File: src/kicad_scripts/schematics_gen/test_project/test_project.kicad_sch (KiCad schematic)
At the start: 102 parts

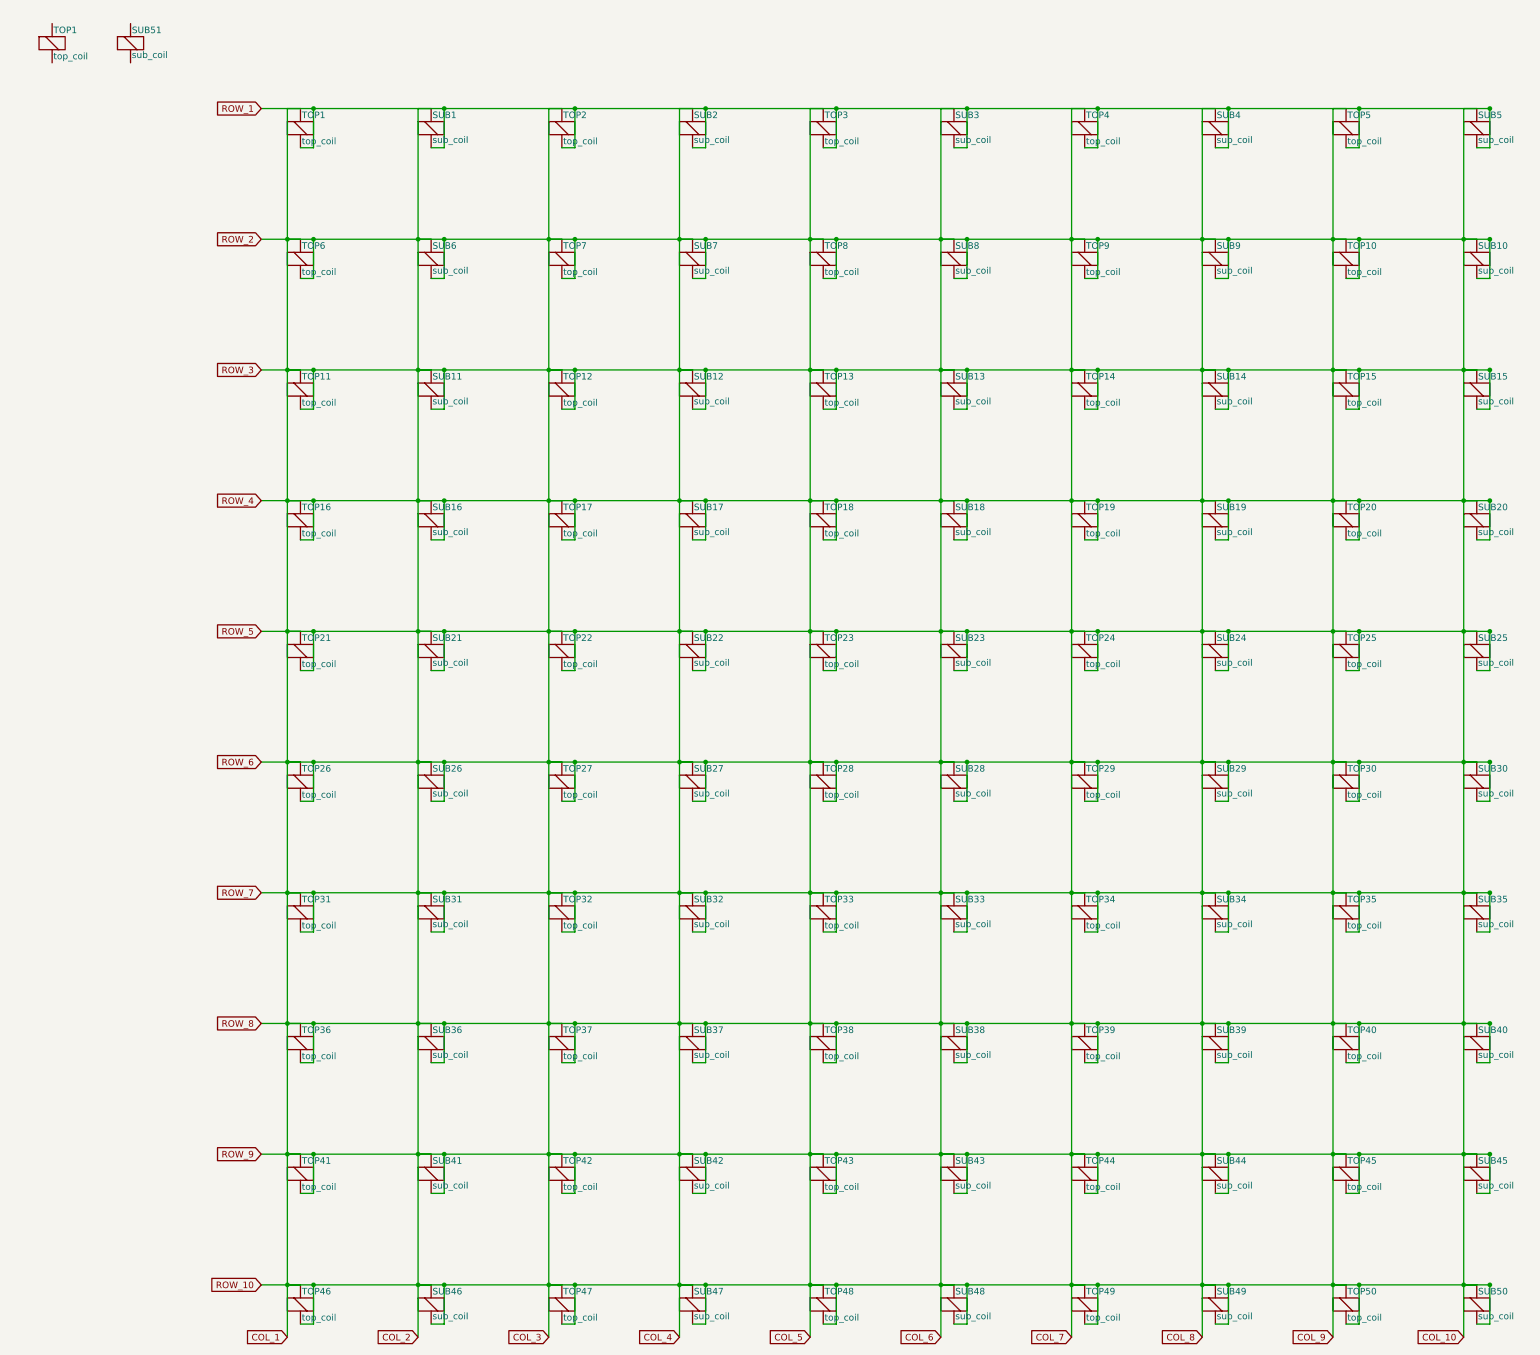
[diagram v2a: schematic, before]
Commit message: Working component matrix schematics drawer
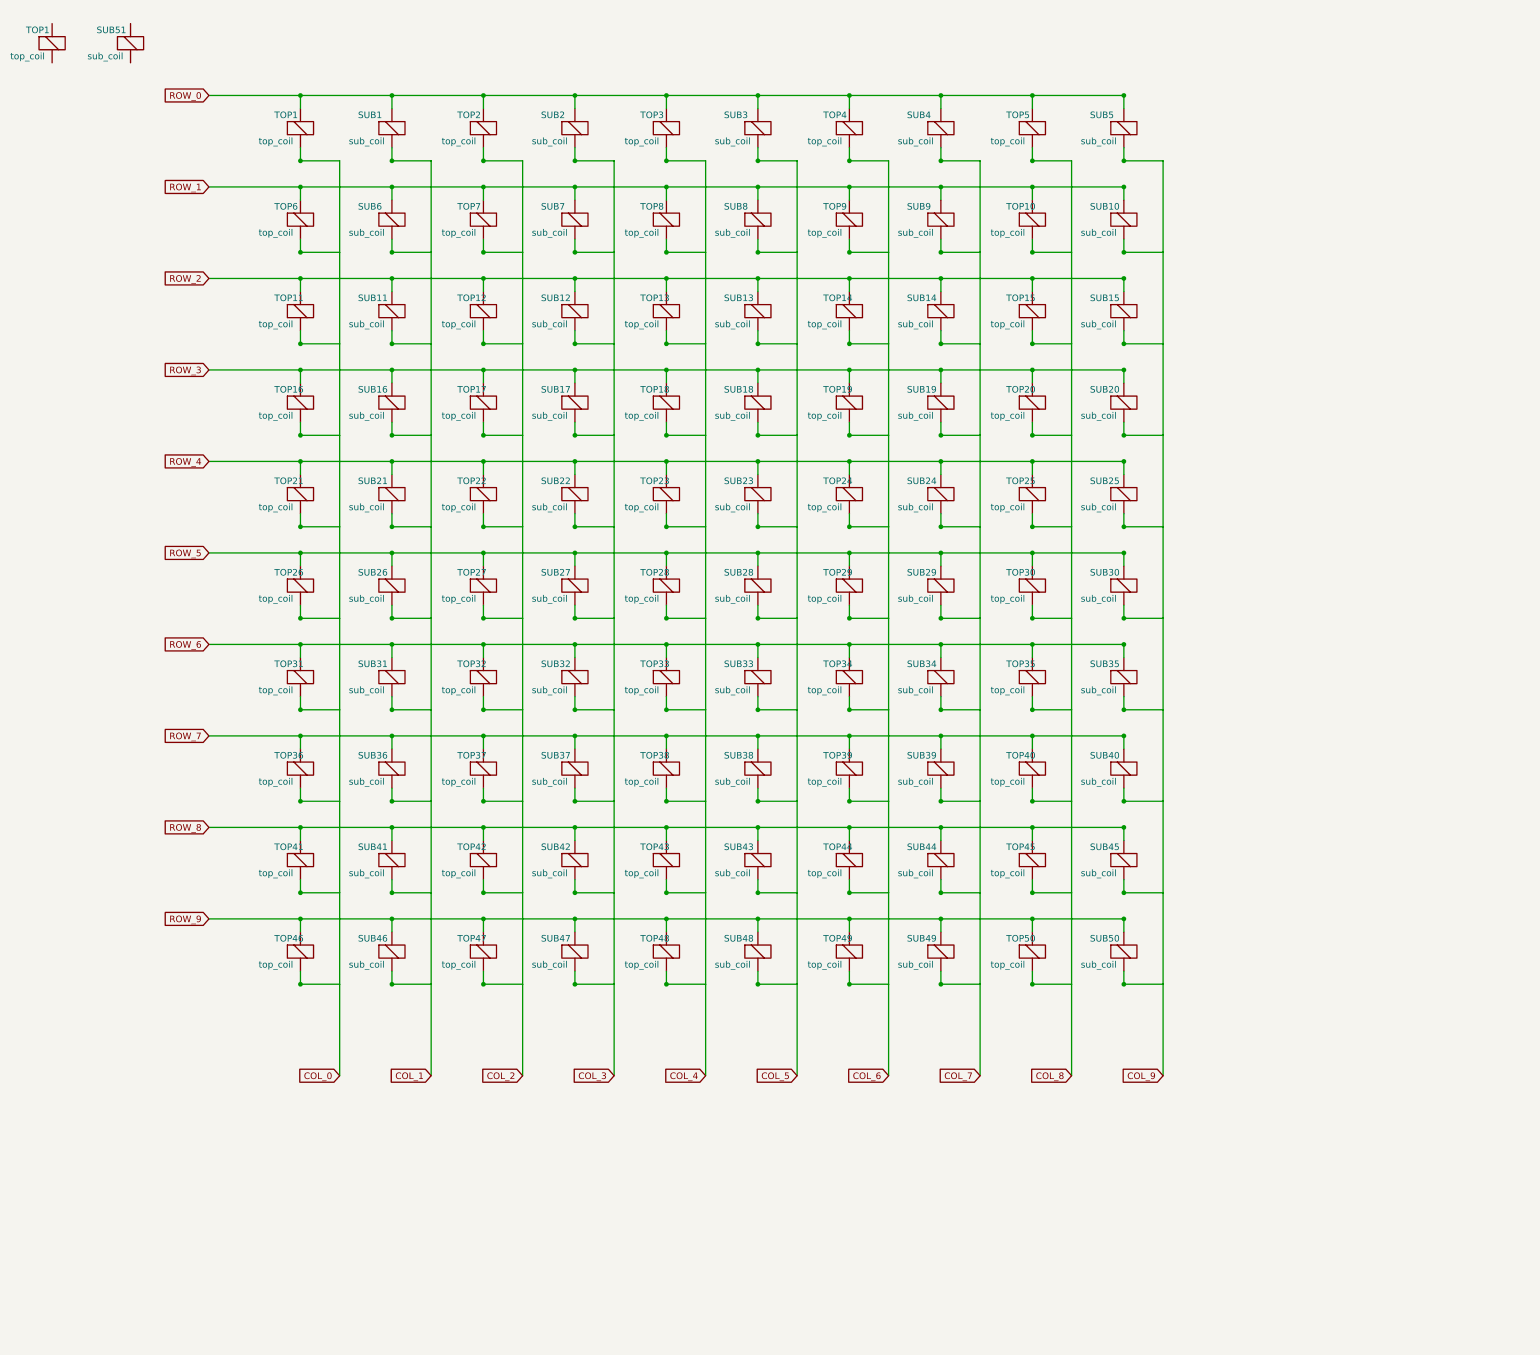
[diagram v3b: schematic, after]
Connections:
- net COL_1: no longer SUB1.1 (A), SUB10.1 (A), SUB10.2 (B), SUB11.1 (A), SUB12.1 (A), SUB12.2 (B), SUB13.1 (A), SUB13.2 (B), SUB14.1 (A), SUB14.2 (B), SUB15.1 (A), SUB15.2 (B), SUB16.1 (A), SUB17.1 (A), SUB17.2 (B), SUB18.1 (A), SUB18.2 (B), SUB19.1 (A), SUB19.2 (B), SUB2.1 (A), SUB2.2 (B), SUB20.1 (A), SUB20.2 (B), SUB21.1 (A), SUB22.1 (A), SUB22.2 (B), SUB23.1 (A), SUB23.2 (B), SUB24.1 (A), SUB24.2 (B), SUB25.1 (A), SUB25.2 (B), SUB26.1 (A), SUB27.1 (A), SUB27.2 (B), SUB28.1 (A), SUB28.2 (B), SUB29.1 (A), SUB29.2 (B), SUB3.1 (A), SUB3.2 (B), SUB30.1 (A), SUB30.2 (B), SUB31.1 (A), SUB32.1 (A), SUB32.2 (B), SUB33.1 (A), SUB33.2 (B), SUB34.1 (A), SUB34.2 (B), SUB35.1 (A), SUB35.2 (B), SUB36.1 (A), SUB37.1 (A), SUB37.2 (B), SUB38.1 (A), SUB38.2 (B), SUB39.1 (A), SUB39.2 (B), SUB4.1 (A), SUB4.2 (B), SUB40.1 (A), SUB40.2 (B), SUB41.1 (A), SUB42.1 (A), SUB42.2 (B), SUB43.1 (A), SUB43.2 (B), SUB44.1 (A), SUB44.2 (B), SUB45.1 (A), SUB45.2 (B), SUB46.1 (A), SUB47.1 (A), SUB47.2 (B), SUB48.1 (A), SUB48.2 (B), SUB49.1 (A), SUB49.2 (B), SUB5.1 (A), SUB5.2 (B), SUB50.1 (A), SUB50.2 (B), SUB6.1 (A), SUB7.1 (A), SUB7.2 (B), SUB8.1 (A), SUB8.2 (B), SUB9.1 (A), SUB9.2 (B), TOP1.1 (A), TOP1.2 (B), TOP10.1 (A), TOP10.2 (B), TOP11.1 (A), TOP11.2 (B), TOP12.1 (A), TOP12.2 (B), TOP13.1 (A), TOP13.2 (B), TOP14.1 (A), TOP14.2 (B), TOP15.1 (A), TOP15.2 (B), TOP16.1 (A), TOP16.2 (B), TOP17.1 (A), TOP17.2 (B), TOP18.1 (A), TOP18.2 (B), TOP19.1 (A), TOP19.2 (B), TOP2.1 (A), TOP2.2 (B), TOP20.1 (A), TOP20.2 (B), TOP21.1 (A), TOP21.2 (B), TOP22.1 (A), TOP22.2 (B), TOP23.1 (A), TOP23.2 (B), TOP24.1 (A), TOP24.2 (B), TOP25.1 (A), TOP25.2 (B), TOP26.1 (A), TOP26.2 (B), TOP27.1 (A), TOP27.2 (B), TOP28.1 (A), TOP28.2 (B), TOP29.1 (A), TOP29.2 (B), TOP3.1 (A), TOP3.2 (B), TOP30.1 (A), TOP30.2 (B), TOP31.1 (A), TOP31.2 (B), TOP32.1 (A), TOP32.2 (B), TOP33.1 (A), TOP33.2 (B), TOP34.1 (A), TOP34.2 (B), TOP35.1 (A), TOP35.2 (B), TOP36.1 (A), TOP36.2 (B), TOP37.1 (A), TOP37.2 (B), TOP38.1 (A), TOP38.2 (B), TOP39.1 (A), TOP39.2 (B), TOP4.1 (A), TOP4.2 (B), TOP40.1 (A), TOP40.2 (B), TOP41.1 (A), TOP41.2 (B), TOP42.1 (A), TOP42.2 (B), TOP43.1 (A), TOP43.2 (B), TOP44.1 (A), TOP44.2 (B), TOP45.1 (A), TOP45.2 (B), TOP46.1 (A), TOP46.2 (B), TOP47.1 (A), TOP47.2 (B), TOP48.1 (A), TOP48.2 (B), TOP49.1 (A), TOP49.2 (B), TOP5.1 (A), TOP5.2 (B), TOP50.1 (A), TOP50.2 (B), TOP6.1 (A), TOP6.2 (B), TOP7.1 (A), TOP7.2 (B), TOP8.1 (A), TOP8.2 (B), TOP9.1 (A), TOP9.2 (B)
- new net COL_0: TOP1.2 (B), TOP11.2 (B), TOP16.2 (B), TOP21.2 (B), TOP26.2 (B), TOP31.2 (B), TOP36.2 (B), TOP41.2 (B), TOP46.2 (B), TOP6.2 (B)
- new net COL_2: TOP12.2 (B), TOP17.2 (B), TOP2.2 (B), TOP22.2 (B), TOP27.2 (B), TOP32.2 (B), TOP37.2 (B), TOP42.2 (B), TOP47.2 (B), TOP7.2 (B)
- new net COL_3: SUB12.2 (B), SUB17.2 (B), SUB2.2 (B), SUB22.2 (B), SUB27.2 (B), SUB32.2 (B), SUB37.2 (B), SUB42.2 (B), SUB47.2 (B), SUB7.2 (B)
- new net COL_4: TOP13.2 (B), TOP18.2 (B), TOP23.2 (B), TOP28.2 (B), TOP3.2 (B), TOP33.2 (B), TOP38.2 (B), TOP43.2 (B), TOP48.2 (B), TOP8.2 (B)
- new net COL_5: SUB13.2 (B), SUB18.2 (B), SUB23.2 (B), SUB28.2 (B), SUB3.2 (B), SUB33.2 (B), SUB38.2 (B), SUB43.2 (B), SUB48.2 (B), SUB8.2 (B)
- new net COL_6: TOP14.2 (B), TOP19.2 (B), TOP24.2 (B), TOP29.2 (B), TOP34.2 (B), TOP39.2 (B), TOP4.2 (B), TOP44.2 (B), TOP49.2 (B), TOP9.2 (B)
- new net COL_7: SUB14.2 (B), SUB19.2 (B), SUB24.2 (B), SUB29.2 (B), SUB34.2 (B), SUB39.2 (B), SUB4.2 (B), SUB44.2 (B), SUB49.2 (B), SUB9.2 (B)
- new net COL_8: TOP10.2 (B), TOP15.2 (B), TOP20.2 (B), TOP25.2 (B), TOP30.2 (B), TOP35.2 (B), TOP40.2 (B), TOP45.2 (B), TOP5.2 (B), TOP50.2 (B)
- new net COL_9: SUB10.2 (B), SUB15.2 (B), SUB20.2 (B), SUB25.2 (B), SUB30.2 (B), SUB35.2 (B), SUB40.2 (B), SUB45.2 (B), SUB5.2 (B), SUB50.2 (B)
- new net ROW_0: SUB1.1 (A), SUB2.1 (A), SUB3.1 (A), SUB4.1 (A), SUB5.1 (A), TOP1.1 (A), TOP2.1 (A), TOP3.1 (A), TOP4.1 (A), TOP5.1 (A)
- new net ROW_1: SUB10.1 (A), SUB6.1 (A), SUB7.1 (A), SUB8.1 (A), SUB9.1 (A), TOP10.1 (A), TOP6.1 (A), TOP7.1 (A), TOP8.1 (A), TOP9.1 (A)
- new net ROW_2: SUB11.1 (A), SUB12.1 (A), SUB13.1 (A), SUB14.1 (A), SUB15.1 (A), TOP11.1 (A), TOP12.1 (A), TOP13.1 (A), TOP14.1 (A), TOP15.1 (A)
- new net ROW_3: SUB16.1 (A), SUB17.1 (A), SUB18.1 (A), SUB19.1 (A), SUB20.1 (A), TOP16.1 (A), TOP17.1 (A), TOP18.1 (A), TOP19.1 (A), TOP20.1 (A)
- new net ROW_4: SUB21.1 (A), SUB22.1 (A), SUB23.1 (A), SUB24.1 (A), SUB25.1 (A), TOP21.1 (A), TOP22.1 (A), TOP23.1 (A), TOP24.1 (A), TOP25.1 (A)
- new net ROW_5: SUB26.1 (A), SUB27.1 (A), SUB28.1 (A), SUB29.1 (A), SUB30.1 (A), TOP26.1 (A), TOP27.1 (A), TOP28.1 (A), TOP29.1 (A), TOP30.1 (A)
- new net ROW_6: SUB31.1 (A), SUB32.1 (A), SUB33.1 (A), SUB34.1 (A), SUB35.1 (A), TOP31.1 (A), TOP32.1 (A), TOP33.1 (A), TOP34.1 (A), TOP35.1 (A)
- new net ROW_7: SUB36.1 (A), SUB37.1 (A), SUB38.1 (A), SUB39.1 (A), SUB40.1 (A), TOP36.1 (A), TOP37.1 (A), TOP38.1 (A), TOP39.1 (A), TOP40.1 (A)
- new net ROW_8: SUB41.1 (A), SUB42.1 (A), SUB43.1 (A), SUB44.1 (A), SUB45.1 (A), TOP41.1 (A), TOP42.1 (A), TOP43.1 (A), TOP44.1 (A), TOP45.1 (A)
- new net ROW_9: SUB46.1 (A), SUB47.1 (A), SUB48.1 (A), SUB49.1 (A), SUB50.1 (A), TOP46.1 (A), TOP47.1 (A), TOP48.1 (A), TOP49.1 (A), TOP50.1 (A)

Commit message: Fixed scalability issue
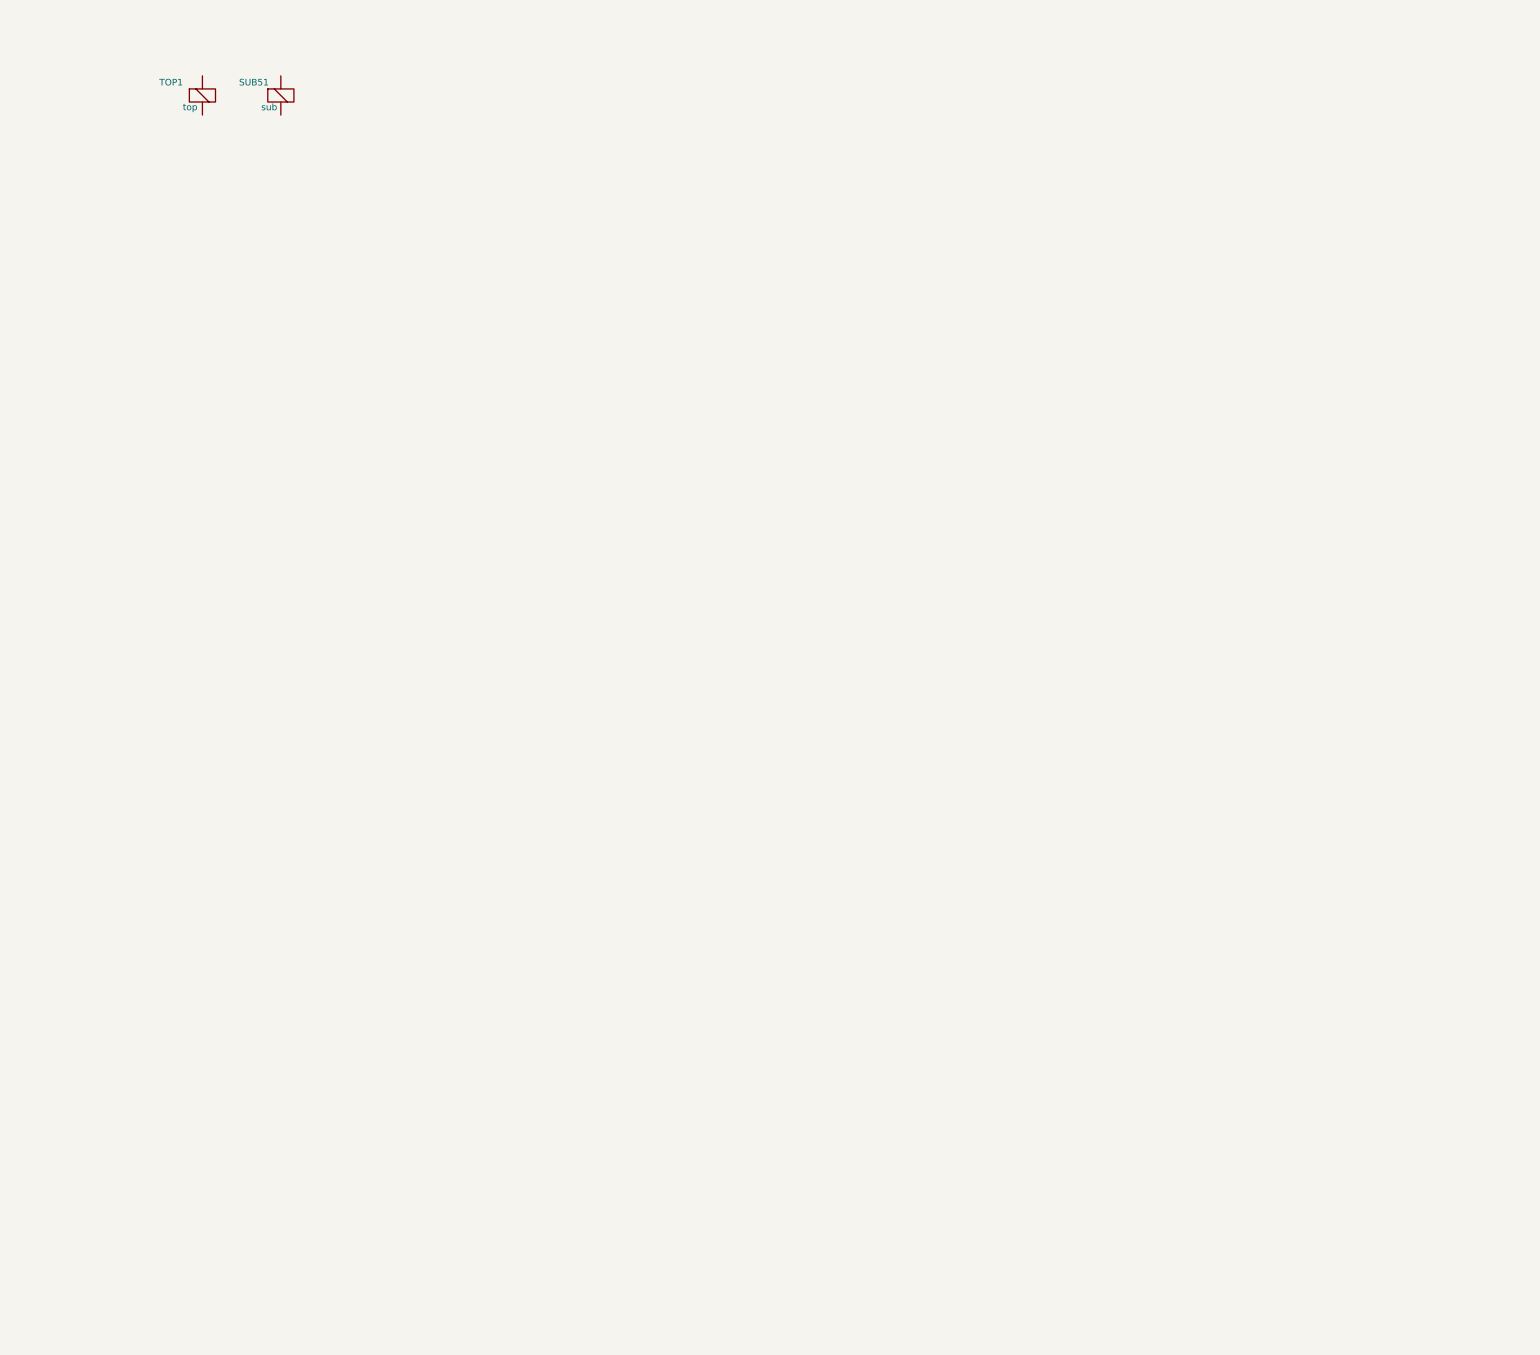
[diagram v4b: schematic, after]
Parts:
- removed SUB1, SUB10, SUB11, SUB12, SUB13, SUB14, SUB15, SUB16, SUB17, SUB18, SUB19, SUB2, SUB20, SUB21, SUB22, SUB23, SUB24, SUB25, SUB26, SUB27, SUB28, SUB29, SUB3, SUB30, SUB31, SUB32, SUB33, SUB34, SUB35, SUB36, SUB37, SUB38, SUB39, SUB4, SUB40, SUB41, SUB42, SUB43, SUB44, SUB45, SUB46, SUB47, SUB48, SUB49, SUB5, SUB50, SUB6, SUB7, SUB8, SUB9: sub_coil, sub_coils:top_coil, symbol square_coils:sub_coil
- removed TOP1, TOP10, TOP11, TOP12, TOP13, TOP14, TOP15, TOP16, TOP17, TOP18, TOP19, TOP2, TOP20, TOP21, TOP22, TOP23, TOP24, TOP25, TOP26, TOP27, TOP28, TOP29, TOP3, TOP30, TOP31, TOP32, TOP33, TOP34, TOP35, TOP36, TOP37, TOP38, TOP39, TOP4, TOP40, TOP41, TOP42, TOP43, TOP44, TOP45, TOP46, TOP47, TOP48, TOP49, TOP5, TOP50, TOP6, TOP7, TOP8, TOP9: top_coil, sub_coils:top_coil, symbol square_coils:top_coil
- SUB51: value sub_coil -> sub
- TOP1: value top_coil -> top
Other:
- moved on the sheet: SUB51, TOP1
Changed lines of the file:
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@@
+(kicad_sch
+	(version 20231120)
+	(generator "eeschema")
+	(generator_version "8.0")
+	(paper "A2")
+	(title_block
+		(date "2024-07-23")
+	)
+	(symbol
+		(lib_id "square_coils:sub_coil")
+		(at -5.08 -6.35 0)
+		(unit 1)
+		(exclude_from_sim no)
+		(in_bom yes)
+		(on_board yes)
+		(dnp no)
+		(property "Reference" "SUB51"
+			(at -13.208 -8.89 0)
+			(effects
+				(font
+					(size 1.27 1.27)
+				)
+				(justify left)
+			)
+		)
+		(property "Value" "sub"
+			(at -8.89 -4.064 0)
+			(effects
+				(font
+					(size 1.27 1.27)
+				)
+				(justify left)
+			)
+		)
+		(property "Footprint" "sub_coils:top_coil"
+			(at -11.938 -8.128 90)
+			(effects
+				(font
+					(size 1.27 1.27)
+				)
+				(hide yes)
+			)
+		)
+		(property "Datasheet" "~"
+			(at -5.715 -7.62 90)
+			(effects
+				(font
+					(size 1.27 1.27)
+				)
+				(hide yes)
+			)
+		)
+		(property "Description" "Electromagnetic actor"
+			(at -5.08 -5.08 0)
+			(effects
+				(font
+					(size 1.27 1.27)
+				)
+				(hide yes)
+			)
+		)
+		(pin "1"
+		)
+		(pin "2"
+		)
+		(instances
+			(project ""
+				(path "/11af7b42-8094-4ca6-9444-8e07a1921bec"
+					(reference "SUB51")
+					(unit 1)
+				)
+			)
+		)
+	)
+	(symbol
+		(lib_id "square_coils:top_coil")
+		(at -20.32 -6.35 0)
+		(unit 1)
+		(exclude_from_sim no)
+		(in_bom yes)
+		(on_board yes)
+		(dnp no)
+		(property "Reference" "TOP1"
+			(at -28.702 -8.89 0)
+			(effects
+				(font
+					(size 1.27 1.27)
+				)
+				(justify left)
+			)
+		)
+		(property "Value" "top"
+			(at -24.13 -4.064 0)
+			(effects
+				(font
+					(size 1.27 1.27)
+				)
+				(justify left)
+			)
+		)
+		(property "Footprint" "sub_coils:top_coil"
+			(at -27.178 -9.398 90)
+			(effects
+				(font
+					(size 1.27 1.27)
+				)
+				(hide yes)
+			)
+		)
+		(property "Datasheet" "~"
+			(at -20.955 -8.89 90)
+			(effects
+				(font
+					(size 1.27 1.27)
+				)
+				(hide yes)
+			)
+		)
+		(property "Description" "Electromagnetic actor"
+			(at -20.32 -6.35 0)
+			(effects
+				(font
+					(size 1.27 1.27)
+				)
+				(hide yes)
+			)
+		)
+		(pin "2"
+		)
+		(pin "1"
+		)
+		(instances
+			(project ""
+				(path "/11af7b42-8094-4ca6-9444-8e07a1921bec"
+					(reference "TOP1")
+					(unit 1)
+				)
+			)
+		)
+	)
+	(sheet_instances
+		(path "/"
+			(page "1")
+		)
+	)
+)
